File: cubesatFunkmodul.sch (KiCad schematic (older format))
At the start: 14 parts, among them IC1 74HC4050, U2 ATMEGA128-16AU, Y1 Crystal_GND23

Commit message: Adds new values
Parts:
- removed C1, C2, C3: C, Capacitors_SMD:C_0603, symbol C
- removed C4, C5: 10pF, Capacitors_SMD:C_0603_HandSoldering, symbol C
- removed C6: C, Capacitors_SMD:C_0603_HandSoldering, symbol C
- removed D1: D, Diodes_SMD:D_0603, symbol D
- removed IC1: 74HC4050, Housings_SSOP:SSOP-16_5.3x6.2mm_Pitch0.65mm, symbol 74HC4050
- removed L1: Ferrite_Bead, Inductors_SMD:L_0603_HandSoldering, symbol Ferrite_Bead
- removed R1, R2, R3: R, Resistors_SMD:R_0603_HandSoldering, symbol R
- removed U2: ATMEGA128-16AU, Housings_QFP:TQFP-64_14x14mm_Pitch0.8mm, symbol ATMEGA128-16AU
- removed Y1: Crystal_GND23, Crystals:Crystal_SMD_0603-4pin_6.0x3.5mm_HandSoldering, symbol Crystal_GND23
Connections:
- net labels removed: +3.3V, +3V3, +5V, ATMEGA-RESET, GND, MISO, MOSI, SCK, SS
- wire segments 33 -> 0

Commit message: Adds new submodules
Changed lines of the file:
@@
 LIBS:contrib
 LIBS:valves
-LIBS:nxp-ic
-LIBS:7400-ic
 LIBS:cubesatFunkmodul-cache
 EELAYER 25 0
@@
 $Descr A4 11693 8268
 encoding utf-8
-Sheet 1 2
+Sheet 1 3
 Title ""
 Date ""
@@
 F1 "Funkmodul1.sch" 60
 F2 "+3.3V" I R 2050 3000 60
-F3 "+5V" I R 2050 3100 60
-F4 "GND" I R 2050 3200 60
+F3 "GND" I R 2050 3200 60
 $EndSheet
 $EndSCHEMATC

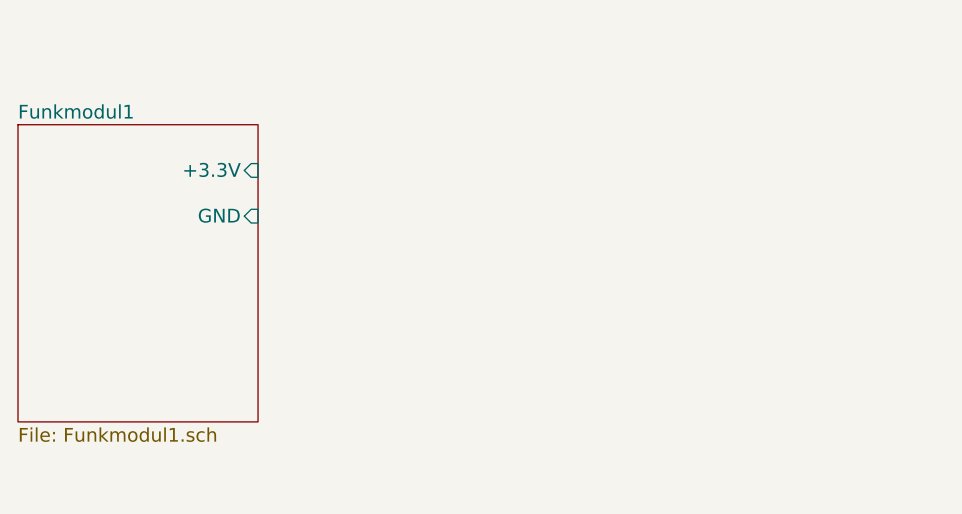
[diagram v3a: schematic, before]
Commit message: Adds ESD Protection and finalisation of wdt
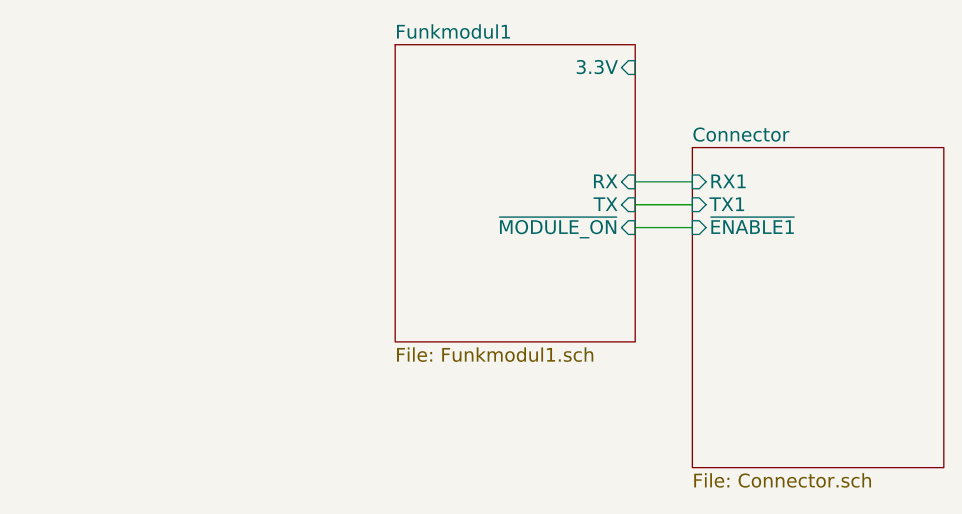
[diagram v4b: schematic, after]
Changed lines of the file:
@@
 $Descr A4 11693 8268
 encoding utf-8
-Sheet 1 3
+Sheet 1 4
 Title ""
 Date ""
@@
 $EndDescr
 $Sheet
-S 1000 2800 1050 1300
+S 2650 2450 1050 1300
 U 5993797A
 F0 "Funkmodul1" 60
 F1 "Funkmodul1.sch" 60
-F2 "+3.3V" I R 2050 3000 60
-F3 "GND" I R 2050 3200 60
+F2 "RX" I R 3700 3050 60
+F3 "TX" I R 3700 3150 60
+F4 "3.3V" I R 3700 2550 60
+F5 "~MODULE_ON~" I R 3700 3250 60
 $EndSheet
+$Sheet
+S 3950 2900 1100 1400
+U 59C45183
+F0 "Connector" 60
+F1 "Connector.sch" 60
+F2 "RX1" I L 3950 3050 60
+F3 "TX1" I L 3950 3150 60
+F4 "~ENABLE1~" I L 3950 3250 60
+$EndSheet
+Wire Wire Line
+	3700 3050 3950 3050
+Wire Wire Line
+	3700 3150 3950 3150
+Wire Wire Line
+	3700 3250 3950 3250
 $EndSCHEMATC

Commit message: Auto stash before merge of "master" and "github/master"
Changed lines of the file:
@@
 LIBS:cubesatFunkmodul-cache
 LIBS:funkmodul
+LIBS:DISCO_Connector
 EELAYER 25 0
 EELAYER END
@@
 F4 "3.3V" I R 3700 2550 60
 F5 "~MODULE_ON~" I R 3700 3250 60
+F6 "TCK" I L 2650 2700 60
+F7 "TMS" I L 2650 2800 60
+F8 "TDO" I L 2650 3000 60
+F9 "TDI" I L 2650 2900 60
+F10 "BAT_OK" I R 3700 2800 60
 $EndSheet
 $Sheet
-S 3950 2900 1100 1400
+S 4900 2400 1100 1400
 U 59C45183
 F0 "Connector" 60
 F1 "Connector.sch" 60
-F2 "RX1" I L 3950 3050 60
-F3 "TX1" I L 3950 3150 60
-F4 "~ENABLE1~" I L 3950 3250 60
+F2 "RX1" I L 4900 3050 60
+F3 "TX1" I L 4900 3150 60
+F4 "~ENABLE1~" I L 4900 3250 60
+F5 "RX2" I R 6000 3050 60
+F6 "TX2" I R 6000 3150 60
+F7 "~ENABLE2~" I R 6000 3250 60
+F8 "3.3V" I L 4900 2550 60
+F9 "BAT_OK" I L 4900 2800 60
 $EndSheet
 Wire Wire Line
-	3700 3050 3950 3050
+	3700 3050 4900 3050
 Wire Wire Line
-	3700 3150 3950 3150
+	3700 3150 4900 3150
 Wire Wire Line
-	3700 3250 3950 3250
+	3700 3250 4900 3250
+Wire Wire Line
+	3700 2550 4900 2550
+Wire Wire Line
+	3700 2800 4900 2800
 $EndSCHEMATC
